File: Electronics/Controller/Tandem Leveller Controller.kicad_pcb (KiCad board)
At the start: 2 copper layers, 212 x 145 mm, 139 parts, among them J1 Conn_01x02, J10 CAN BUS, J11 TRACTOR BATTERY, J12 PWR SWITCH, J13 VALVE POWER, J14 TABLET 1 PWR, J15 TABLET 2 PWR, J16 SLAVE TABLET, J17 MASTER TABLET, J18 292303-7, J19 292303-7, J2 GPS SIM, J20 FRONT HEIGHT, J21 REAR HEIGHT, J23 CAN, J24 CAN BUS, J25 CAN BUS, J3 Conn_01x02, J4 Conn_01x02, J5 Conn_01x02, J6 Conn_01x02, J7 Conn_01x02, J8 Conn_01x02, J9 TERM, U1 TEENSY 4.0, U10 FT232RL, U11 FT232RL, U12 FT232RL, U13 FT232RL, U14 FT232RL, U15 FT232RL, U16 USB2517, U17 MIC2026-1YM, U2 simpleRTK2B, U3 simpleRTK2B, U4 simpleRTK2B, U5 TJA1462ATK-0Z, U6 PESD2CANFD24V-TR, U7 LM2596S-5, U8 LM2587S-ADJ/NOPB, U9 LM2587S-ADJ/NOPB, Y1 FA-238 24.0000MD30X-W5

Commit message: Added fiducials to all boards.
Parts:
- added FID1: Fiducial, Fiducial:Fiducial_0.5mm_Mask1mm, F.Cu at (68.8, 29.4)
- added FID2: Fiducial, Fiducial:Fiducial_0.5mm_Mask1mm, F.Cu at (254.0, 29.4)
- added FID3: Fiducial, Fiducial:Fiducial_0.5mm_Mask1mm, F.Cu at (63.0, 156.2)
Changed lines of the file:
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@@
     (descr "Capacitor SMD 0805 (2012 Metric), square (rectangular) end terminal, IPC_7351 nominal, (Body size source: IPC-SM-782 page 76, https://www.pcb-3d.com/wordpress/wp-content/uploads/ipc-sm-782a_amendment_1_and_2.pdf, https://docs.google.com/spreadsheets/d/1BsfQQcO9C6DZCsRaXUlFlo91Tg2WpOkGARC1WS5S8t0/edit?usp=sharing), generated with kicad-footprint-generator")
     (tags "capacitor")
-    (property "LCSC" "")
+    (property "LCSC" "C1779")
     (property "Sheetfile" "Slave Tablet.kicad_sch")
     (property "Sheetname" "Slave Tablet")
@@
     (descr "Capacitor SMD 0805 (2012 Metric), square (rectangular) end terminal, IPC_7351 nominal, (Body size source: IPC-SM-782 page 76, https://www.pcb-3d.com/wordpress/wp-content/uploads/ipc-sm-782a_amendment_1_and_2.pdf, https://docs.google.com/spreadsheets/d/1BsfQQcO9C6DZCsRaXUlFlo91Tg2WpOkGARC1WS5S8t0/edit?usp=sharing), generated with kicad-footprint-generator")
     (tags "capacitor")
-    (property "LCSC" "")
+    (property "LCSC" "C1779")
     (property "Sheetfile" "Slave Tablet.kicad_sch")
     (property "Sheetname" "Slave Tablet")
@@
     )
   )
+  (footprint "Fiducial:Fiducial_0.5mm_Mask1mm" (layer "F.Cu")
+    (at 68.8 29.4)
+    (descr "Circular Fiducial, 0.5mm bare copper, 1mm soldermask opening (Level C)")
+    (tags "fiducial")
+    (property "Sheetfile" "Tandem Leveller Controller.kicad_sch")
+    (property "Sheetname" "")
+    (property "ki_description" "Fiducial Marker")
+    (property "ki_keywords" "fiducial marker")
+    (attr smd)
+    (fp_text reference "FID1" (at 0 -1.5) (layer "F.SilkS") hide
+        (effects (font (size 1 1) (thickness 0.15)))
+    )
+    (fp_text value "Fiducial" (at 0 1.5) (layer "F.Fab")
+        (effects (font (size 1 1) (thickness 0.15)))
+    )
+    (fp_text user "${REFERENCE}" (at 0 0) (layer "F.Fab")
+        (effects (font (size 0.2 0.2) (thickness 0.04)))
+    )
+    (fp_circle (center 0 0) (end 0.75 0)
+      (stroke (width 0.05) (type solid)) (fill none) (layer "F.CrtYd"))
+    (fp_circle (center 0 0) (end 0.5 0)
+      (stroke (width 0.1) (type solid)) (fill none) (layer "F.Fab"))
+    (pad "" smd circle (at 0 0) (size 0.5 0.5) (layers "F.Cu" "F.Mask")
+      (solder_mask_margin 0.25) (clearance 0.25))
+  )
   (footprint "Resistor_SMD:R_0805_2012Metric" (layer "F.Cu")
     (at 225.525 160.6 -90)
@@
     (descr "Capacitor SMD 0805 (2012 Metric), square (rectangular) end terminal, IPC_7351 nominal, (Body size source: IPC-SM-782 page 76, https://www.pcb-3d.com/wordpress/wp-content/uploads/ipc-sm-782a_amendment_1_and_2.pdf, https://docs.google.com/spreadsheets/d/1BsfQQcO9C6DZCsRaXUlFlo91Tg2WpOkGARC1WS5S8t0/edit?usp=sharing), generated with kicad-footprint-generator")
     (tags "capacitor")
-    (property "LCSC" "")
+    (property "LCSC" "C1779")
     (property "Sheetfile" "USB Devices.kicad_sch")
     (property "Sheetname" "USB Devices")
@@
     (descr "Capacitor SMD 0805 (2012 Metric), square (rectangular) end terminal, IPC_7351 nominal, (Body size source: IPC-SM-782 page 76, https://www.pcb-3d.com/wordpress/wp-content/uploads/ipc-sm-782a_amendment_1_and_2.pdf, https://docs.google.com/spreadsheets/d/1BsfQQcO9C6DZCsRaXUlFlo91Tg2WpOkGARC1WS5S8t0/edit?usp=sharing), generated with kicad-footprint-generator")
     (tags "capacitor")
-    (property "LCSC" "")
+    (property "LCSC" "C1779")
     (property "Sheetfile" "USB Devices.kicad_sch")
     (property "Sheetname" "USB Devices")
@@
     )
   )
+  (footprint "Fiducial:Fiducial_0.5mm_Mask1mm" (layer "F.Cu")
+    (at 254 29.4)
+    (descr "Circular Fiducial, 0.5mm bare copper, 1mm soldermask opening (Level C)")
+    (tags "fiducial")
+    (property "Sheetfile" "Tandem Leveller Controller.kicad_sch")
+    (property "Sheetname" "")
+    (property "ki_description" "Fiducial Marker")
+    (property "ki_keywords" "fiducial marker")
+    (attr smd)
+    (fp_text reference "FID2" (at 0 -1.5) (layer "F.SilkS") hide
+        (effects (font (size 1 1) (thickness 0.15)))
+    )
+    (fp_text value "Fiducial" (at 0 1.5) (layer "F.Fab")
+        (effects (font (size 1 1) (thickness 0.15)))
+    )
+    (fp_text user "${REFERENCE}" (at 0 0) (layer "F.Fab")
+        (effects (font (size 0.2 0.2) (thickness 0.04)))
+    )
+    (fp_circle (center 0 0) (end 0.75 0)
+      (stroke (width 0.05) (type solid)) (fill none) (layer "F.CrtYd"))
+    (fp_circle (center 0 0) (end 0.5 0)
+      (stroke (width 0.1) (type solid)) (fill none) (layer "F.Fab"))
+    (pad "" smd circle (at 0 0) (size 0.5 0.5) (layers "F.Cu" "F.Mask")
+      (solder_mask_margin 0.25) (clearance 0.25))
+  )
   (footprint "Capacitor_SMD:C_0805_2012Metric" (layer "F.Cu")
     (at 227.625 160.6 -90)
@@
     (descr "Capacitor SMD 0805 (2012 Metric), square (rectangular) end terminal, IPC_7351 nominal, (Body size source: IPC-SM-782 page 76, https://www.pcb-3d.com/wordpress/wp-content/uploads/ipc-sm-782a_amendment_1_and_2.pdf, https://docs.google.com/spreadsheets/d/1BsfQQcO9C6DZCsRaXUlFlo91Tg2WpOkGARC1WS5S8t0/edit?usp=sharing), generated with kicad-footprint-generator")
     (tags "capacitor")
-    (property "LCSC" "")
+    (property "LCSC" "C1779")
     (property "Sheetfile" "USB Devices.kicad_sch")
     (property "Sheetname" "USB Devices")
@@
     (descr "Capacitor SMD 0805 (2012 Metric), square (rectangular) end terminal, IPC_7351 nominal, (Body size source: IPC-SM-782 page 76, https://www.pcb-3d.com/wordpress/wp-content/uploads/ipc-sm-782a_amendment_1_and_2.pdf, https://docs.google.com/spreadsheets/d/1BsfQQcO9C6DZCsRaXUlFlo91Tg2WpOkGARC1WS5S8t0/edit?usp=sharing), generated with kicad-footprint-generator")
     (tags "capacitor")
-    (property "LCSC" "")
+    (property "LCSC" "C1779")
     (property "Sheetfile" "USB Devices.kicad_sch")
     (property "Sheetname" "USB Devices")
@@
     )
   )
+  (footprint "Fiducial:Fiducial_0.5mm_Mask1mm" (layer "F.Cu")
+    (at 63 156.2)
+    (descr "Circular Fiducial, 0.5mm bare copper, 1mm soldermask opening (Level C)")
+    (tags "fiducial")
+    (property "Sheetfile" "Tandem Leveller Controller.kicad_sch")
+    (property "Sheetname" "")
+    (property "ki_description" "Fiducial Marker")
+    (property "ki_keywords" "fiducial marker")
+    (attr smd)
+    (fp_text reference "FID3" (at 0 -1.5) (layer "F.SilkS") hide
+        (effects (font (size 1 1) (thickness 0.15)))
+    )
+    (fp_text value "Fiducial" (at 0 1.5) (layer "F.Fab")
+        (effects (font (size 1 1) (thickness 0.15)))
+    )
+    (fp_text user "${REFERENCE}" (at 0 0) (layer "F.Fab")
+        (effects (font (size 0.2 0.2) (thickness 0.04)))
+    )
+    (fp_circle (center 0 0) (end 0.75 0)
+      (stroke (width 0.05) (type solid)) (fill none) (layer "F.CrtYd"))
+    (fp_circle (center 0 0) (end 0.5 0)
+      (stroke (width 0.1) (type solid)) (fill none) (layer "F.Fab"))
+    (pad "" smd circle (at 0 0) (size 0.5 0.5) (layers "F.Cu" "F.Mask")
+      (solder_mask_margin 0.25) (clearance 0.25))
+  )
   (footprint "Capacitor_SMD:C_0805_2012Metric" (layer "F.Cu")
     (at 226.2097 58.49875 -90)
@@
   (footprint "Britishideas:Teensy_4.0" (layer "F.Cu")
     (at 202.8 57.45)
-    (property "LCSC" "C2897377")
+    (property "LCSC" "")
     (property "Sheetfile" "Tandem Leveller Controller.kicad_sch")
     (property "Sheetname" "")

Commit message: Changed four way screw block, USB type A connectors, 33uH inductor and 24MHz crystal to use parts that JLCPCB has in stock.
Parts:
- C44, C45, C5, C6: value 100u -> 1729034
- D1: value HSMS-C190 -> APTD1608SECK
- FB1, FB2: value MI0805K400R-10 -> PZ2012D800-3R0TF
- J18, J19: value 292303-7 -> 292303-1; footprint Connector_USB:USB_A_TE_292303-7_Horizontal -> Britishideas:292303-1
- L2: footprint Britishideas:Chilisin_Power_Inductor_AWVS_808040 -> Britishideas:MWSA0603S-330MT
- Y1: value FA-238 24.0000MD30X-W5 -> CF4024M00012; footprint EmSA:FA-238 -> Britishideas:FA-238
- moved J19 6.37 mm to (215.5, 36.4)
- moved J18 5.37 mm to (241.1, 36.3)
- moved L2 2.70 mm to (89.6, 57.4), turned to -90 degrees
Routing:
- net Net-(J18-GND): track 19.8 -> 18.5 mm
- net Net-(J19-D+): track 50.6 -> 51.8 mm
- net /USB Hub/VBUS7: track 75.6 -> 76.7 mm
- net Net-(J19-D-): track 53.2 -> 54.4 mm
- net Net-(J19-GND): track 20.6 -> 19.5 mm
- net GND: vias 865 -> 868

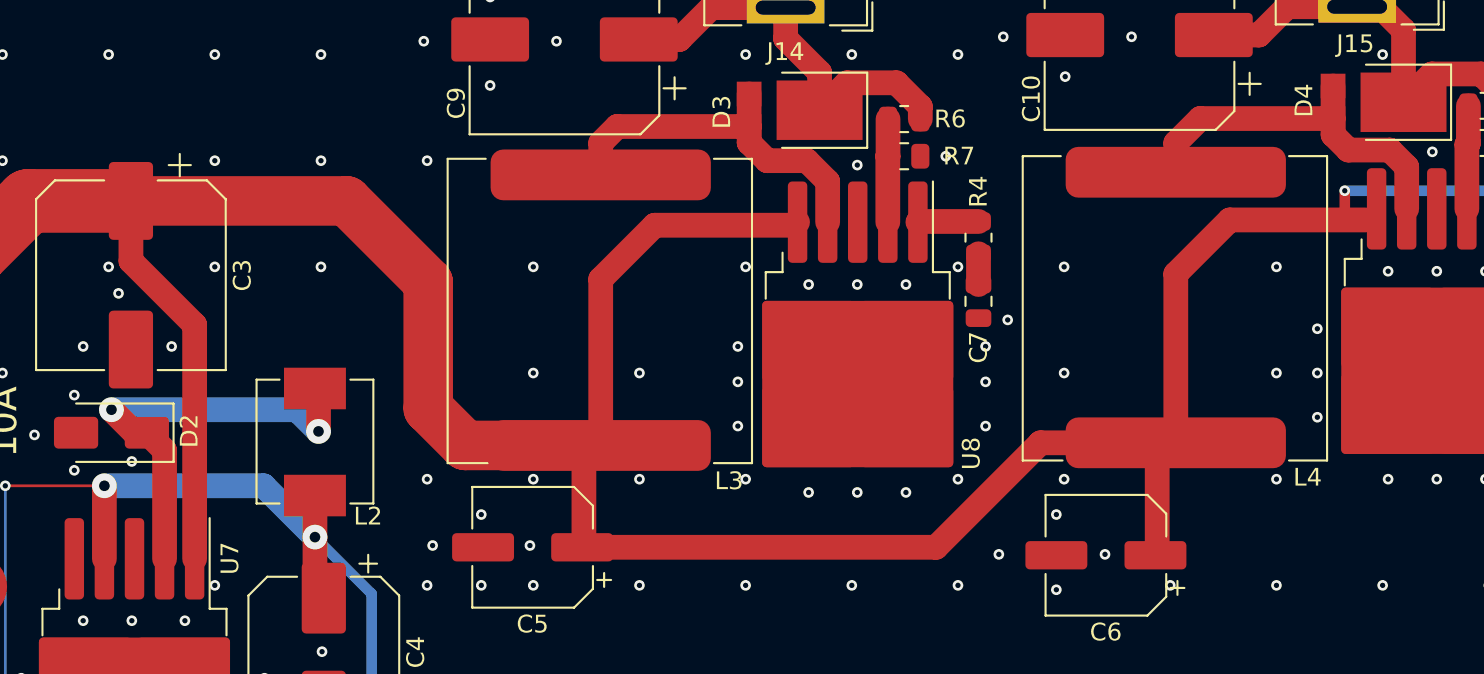
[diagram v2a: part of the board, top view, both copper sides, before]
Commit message: Changed tablet PSU inductors.
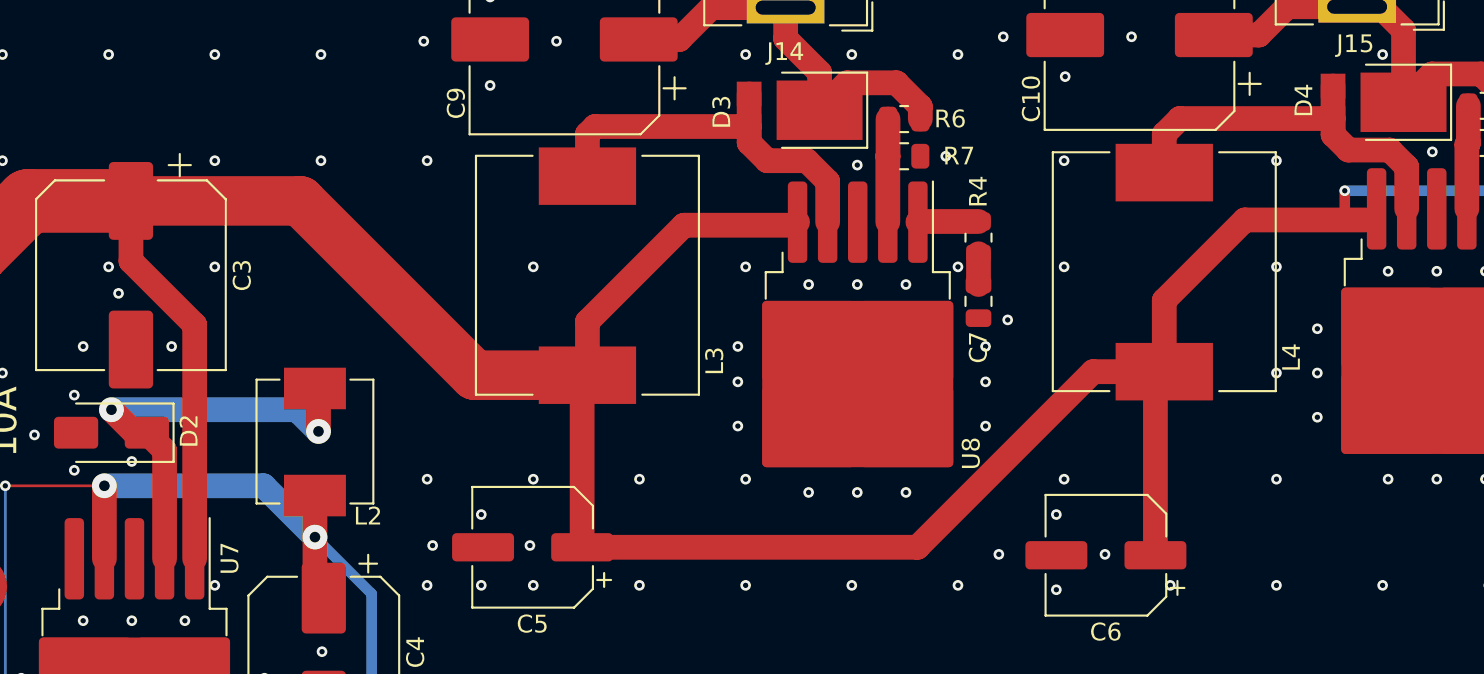
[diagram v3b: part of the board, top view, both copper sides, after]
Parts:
- L3, L4: value IHLP6767DZER470M11 -> MWSA1206S-470MT; footprint Britishideas:IHLP6767DZER470M11 -> Britishideas:MWSA1206S-470MT
- moved L4 4.07 mm to (137.6, 56.4)
- moved L3 4.04 mm to (105.0, 56.6)
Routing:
- net +12V: track 292.3 -> 285.5 mm
- net Net-(D3-A): track 21.0 -> 22.1 mm
- net Net-(D4-A): track 21.2 -> 22.1 mm
- net GND: vias 868 -> 865
